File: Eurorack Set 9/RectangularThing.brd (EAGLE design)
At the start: 99.5 x 100 mm, 180 parts, among them IC1 CEM3310, IC2 TL074D, IC3 CEM3320, IC4 CEM3310, IC5 TL074D, IC7 CEM3340

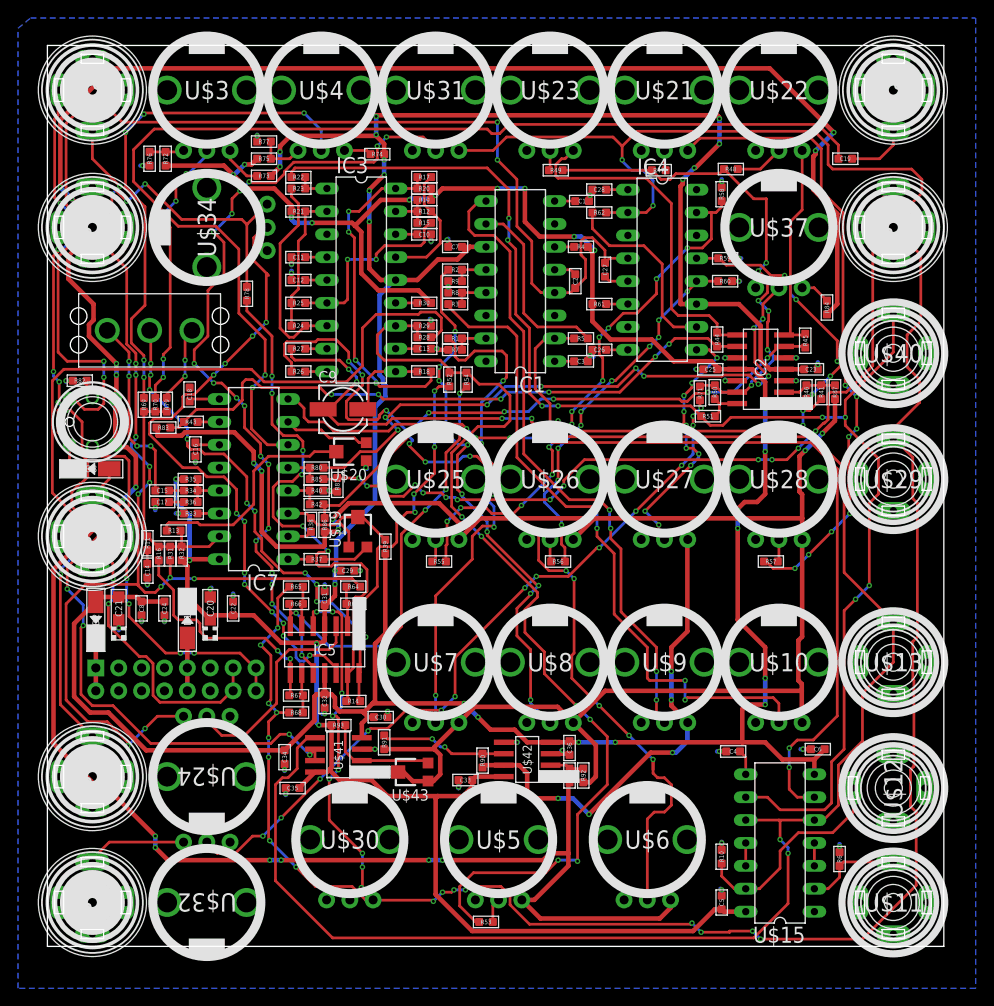
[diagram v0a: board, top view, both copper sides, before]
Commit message: LBR fix and rectangularthing update
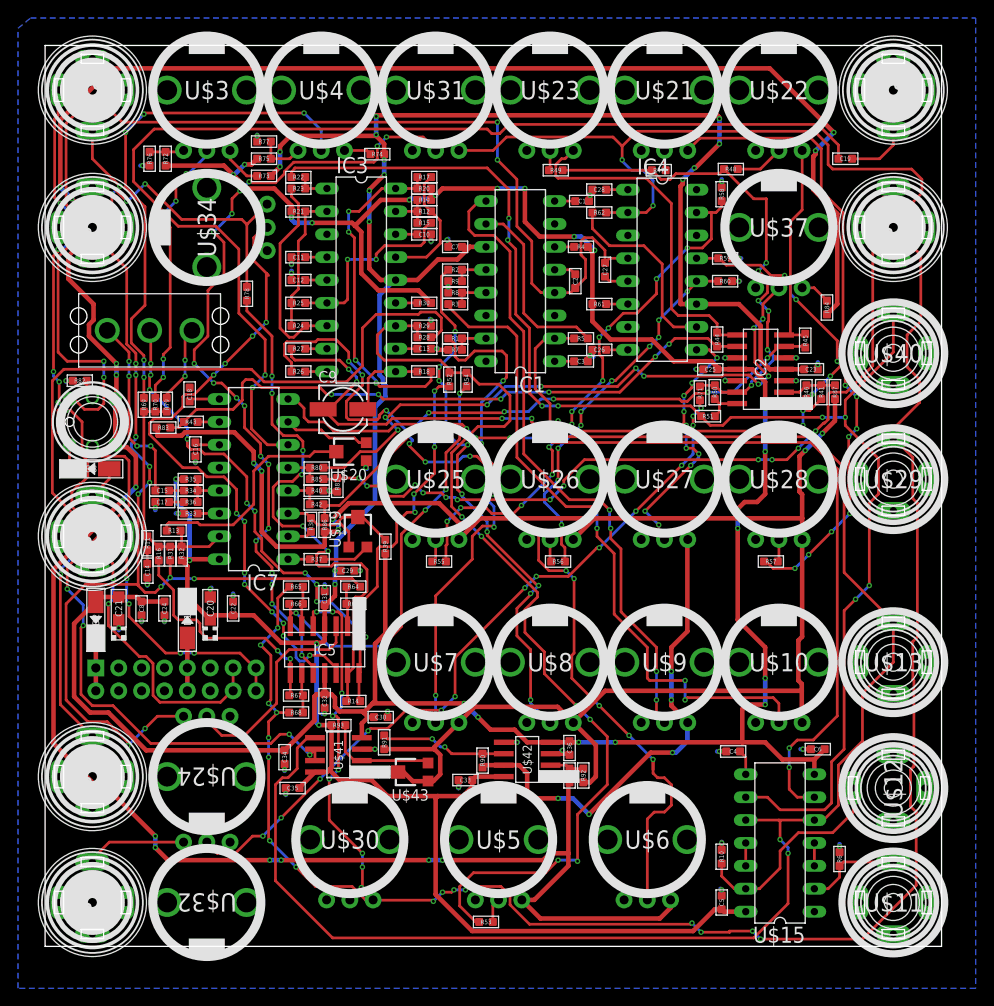
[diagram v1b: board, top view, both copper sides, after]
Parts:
- C20, C21: device EurorackModularParts:AVX-A -> EurorackModularParts:CASE-A_3216
- U$1: value EURORACK_PCB24HP_10X10CM -> EURORACK_PCB20HP_10X10CM; device EurorackModularParts:EURORACK24HP_10X10CM -> EurorackModularParts:EURORACK20HP_10X10CM
- moved U$1 9.91 mm to (-64.0, 11.2)
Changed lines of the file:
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@@
 <layer number="21" name="tPlace" color="7" fill="1" visible="yes" active="yes"/>
 <layer number="22" name="bPlace" color="7" fill="1" visible="yes" active="yes"/>
-<layer number="23" name="tOrigins" color="15" fill="1" visible="no" active="yes"/>
+<layer number="23" name="tOrigins" color="15" fill="1" visible="yes" active="yes"/>
 <layer number="24" name="bOrigins" color="15" fill="1" visible="no" active="yes"/>
 <layer number="25" name="tNames" color="7" fill="1" visible="no" active="yes"/>
@@
 <element name="IC3" library="CEM" package="DIL18" value="CEM3320" x="-28.575" y="88.138" rot="R270"/>
 <element name="IC7" library="CEM" package="DIL16" value="CEM3340" x="-40.513" y="66.04" rot="R90"/>
-<element name="U$1" library="EurorackModularParts" package="EURORACK24HP_10X10CM" value="EURORACK_PCB24HP_10X10CM" x="-73.914" y="11.176"/>
+<element name="U$1" library="EurorackModularParts" package="EURORACK20HP_10X10CM" value="EURORACK_PCB20HP_10X10CM" x="-64.008" y="11.176"/>
 <element name="U$2" library="EurorackModularParts" package="POWER_16_SHROUDED" value="POWERSHROUDED" x="-49.149" y="43.815" rot="MR180"/>
 <element name="U$3" library="EurorackModularParts" package="OG-POTS_ALPS_POT_VERTICAL" value="" x="-45.72" y="109.22">
@@
 <element name="R35" library="OPL" package="R0603" value="1.5M" x="-47.498" y="66.04"/>
 <element name="R36" library="OPL" package="R0603" value="470" x="-47.498" y="63.5" rot="R180"/>
-<element name="C20" library="EurorackModularParts" package="AVX-A" value="10uF" x="-45.339" y="51.689" rot="R90"/>
-<element name="C21" library="EurorackModularParts" package="AVX-A" value="10uF" x="-55.499" y="51.689" rot="R90"/>
+<element name="C20" library="EurorackModularParts" package="CASE-A_3216" value="10uF" x="-45.339" y="51.689" rot="R90"/>
+<element name="C21" library="EurorackModularParts" package="CASE-A_3216" value="10uF" x="-55.499" y="51.689" rot="R90"/>
 <element name="C22" library="OPL" package="C0603" value="100nF" x="-42.799" y="51.689" rot="R90"/>
 <element name="C24" library="OPL" package="C0603" value="100nF" x="-50.419" y="51.689" rot="R90"/>
@@
 <contactref element="C5" pad="1"/>
 <contactref element="C6" pad="2"/>
-<contactref element="C6" pad="2"/>
 <contactref element="C7" pad="1"/>

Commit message: Split schematic over pages
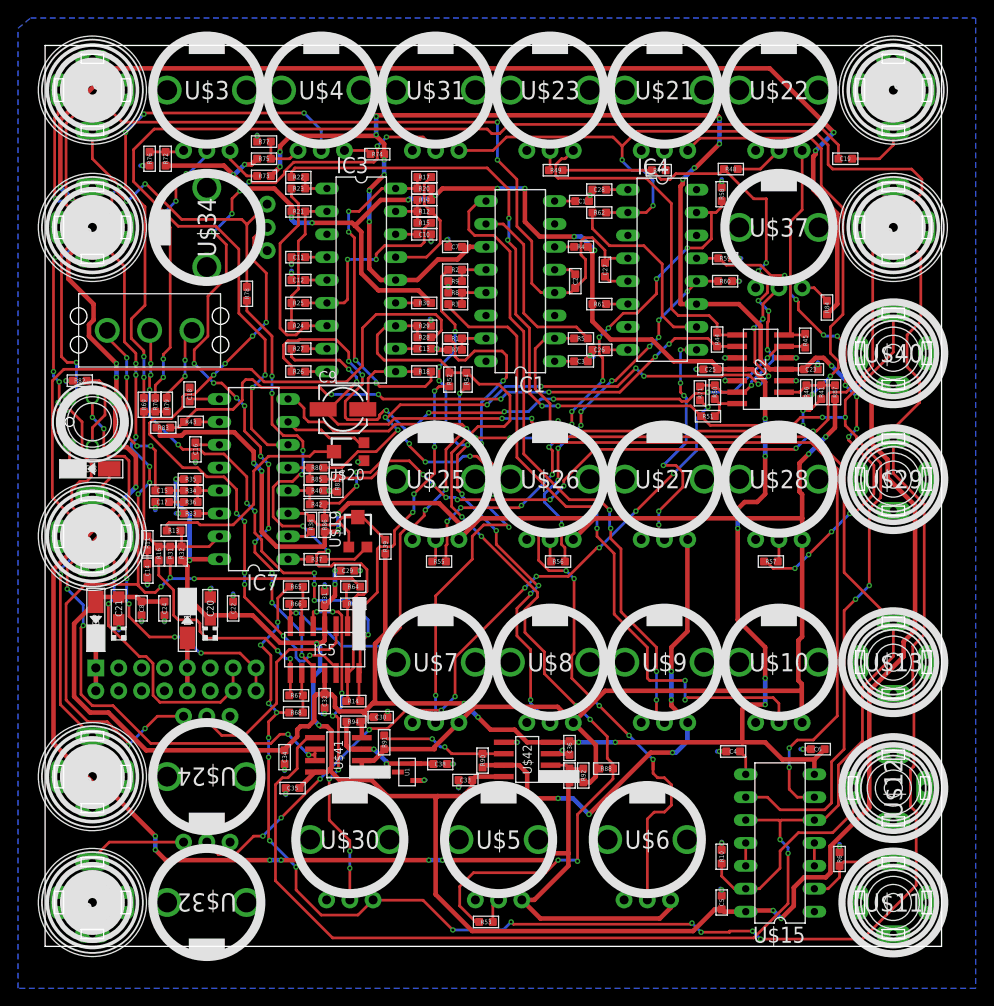
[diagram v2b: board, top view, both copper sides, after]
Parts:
- removed R93: 180, OPL:R0603
- removed U$43: (no value), adafruit:TC33X
- added C38: 100nF, OPL:C0603
- added R88: BIAS, OPL:R0603
- added R94: 10k, OPL:R0603
- added U1: LM4040DIM3-5.0, FarnellThings:SOT95P237X112-3N
- C20, C21: device EurorackModularParts:CASE-A_3216 -> EurorackModularParts:AVX-A
- moved U$20 0.25 mm to (-30.1, 69.1)
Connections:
- removed net N$22: IC3.12, R28.2, R29.1, R52.2, R53.2, R54.2
- removed net N$87: R93.2, U$41.2, U$43.3
- new net -5VIN: C38.2, R94.2, U$41.3, U1.2
- new net CUTOFF_INPUT: IC3.12, R28.2, R29.1, R52.2, R53.2, R54.2, R88.2
- net -12V: now also R94.1
- net -5V: now also R88.1, U$41.2; no longer U$43.1, U$43.2
- net 12V: no longer R93.1
- net GATELED: now also U$39.LEDNEG; no longer U$39.LEDPOS
- net GND: now also C38.1, U1.1; no longer U$41.3
- net N$88: now also U$39.LEDPOS; no longer U$39.LEDNEG
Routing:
- net CUTOFF_INPUT: track 0.00 -> 110.8 mm, vias 0 -> 6
- net N$22: track 110.2 -> 0.00 mm, vias 6 -> 0
- net 12V: track 300.7 -> 346.8 mm, vias 18 -> 22
- net -5VIN: track 0.00 -> 13.4 mm, vias 0 -> 2
- net N$87: track 12.6 -> 0.00 mm
- net -5V: track 203.9 -> 195.7 mm
- net GATE_IN: track 138.9 -> 131.3 mm, vias 4 -> 3
- net N$88: track 2.14 -> 9.51 mm
- net GATELED: track 65.6 -> 70.3 mm, vias 4 -> 6
- net N$60: track 53.1 -> 56.4 mm
- net N$41: track 55.8 -> 58.4 mm
- net A_IN: track 55.7 -> 58.2 mm
- net MODENVOUT: track 268.1 -> 270.5 mm, vias 18 -> 16
- net CV_RACK: track 89.0 -> 90.7 mm, vias 12 -> 10
- net S2_IN: track 28.9 -> 27.3 mm, vias 10 -> 6
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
